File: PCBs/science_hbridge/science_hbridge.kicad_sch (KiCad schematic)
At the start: 34 parts, among them J1 Conn_02x07_Odd_Even, J2 Conn_02x08_Odd_Even, J3 Conn_02x08_Odd_Even, J4 Conn_01x06, J6 Conn_01x02_Pin, J7 Conn_01x04_Pin, J8 Conn_01x06, U1 L298N, U2 MAX485E, U3 NCP718xSN500

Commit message: silkscreen
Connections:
- net 51: no longer R7.2, U2.4 (DI)
- net 52: no longer R12.2, U2.1 (RO)
- net 53: now also R7.2, U2.4 (DI)
- net 54: now also R12.2, U2.1 (RO)
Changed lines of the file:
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@@
 		)
 	)
-	(label "52"
+	(label "54"
 		(at 254 69.85 0)
 		(effects
@@
 		)
 	)
-	(label "51"
+	(label "53"
 		(at 254 77.47 0)
 		(effects

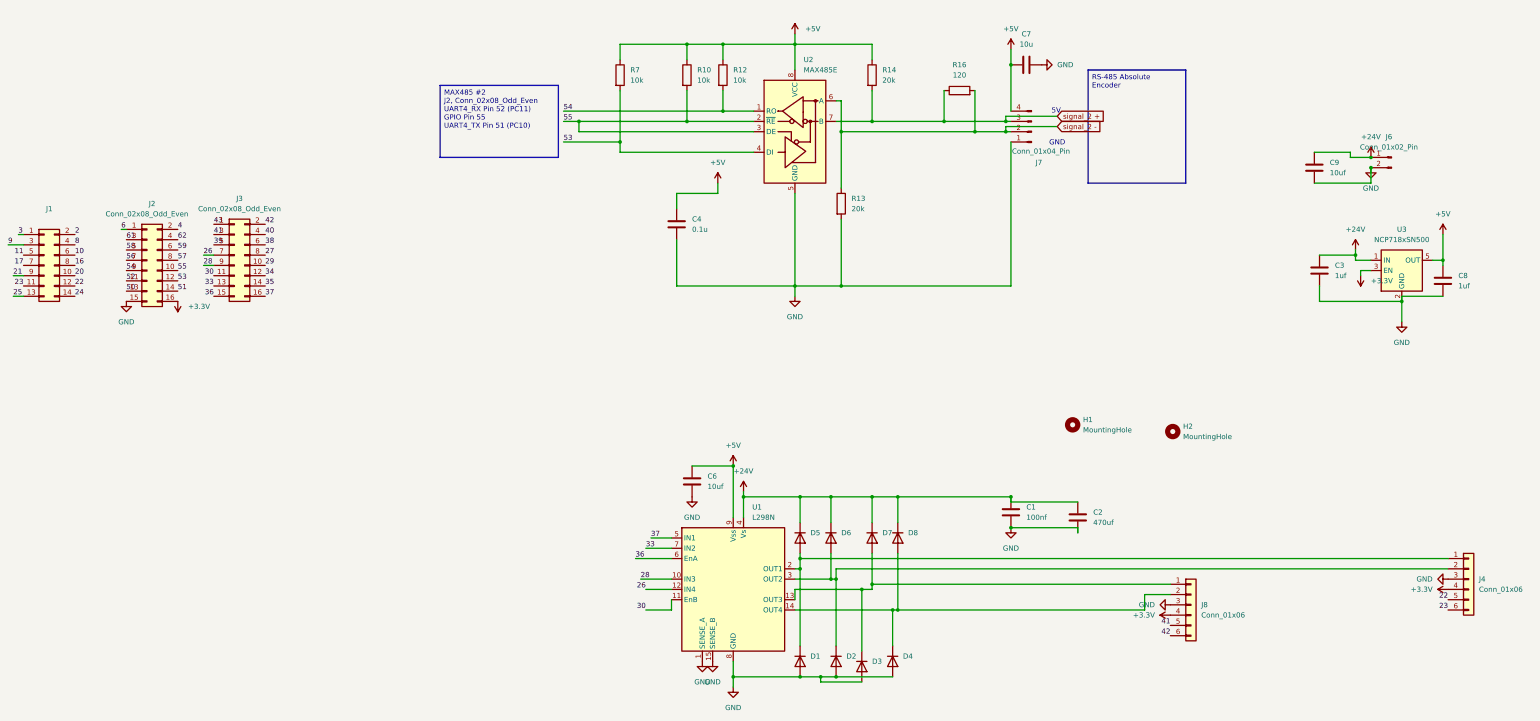
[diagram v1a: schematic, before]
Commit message: fixed 3.3V, fized header
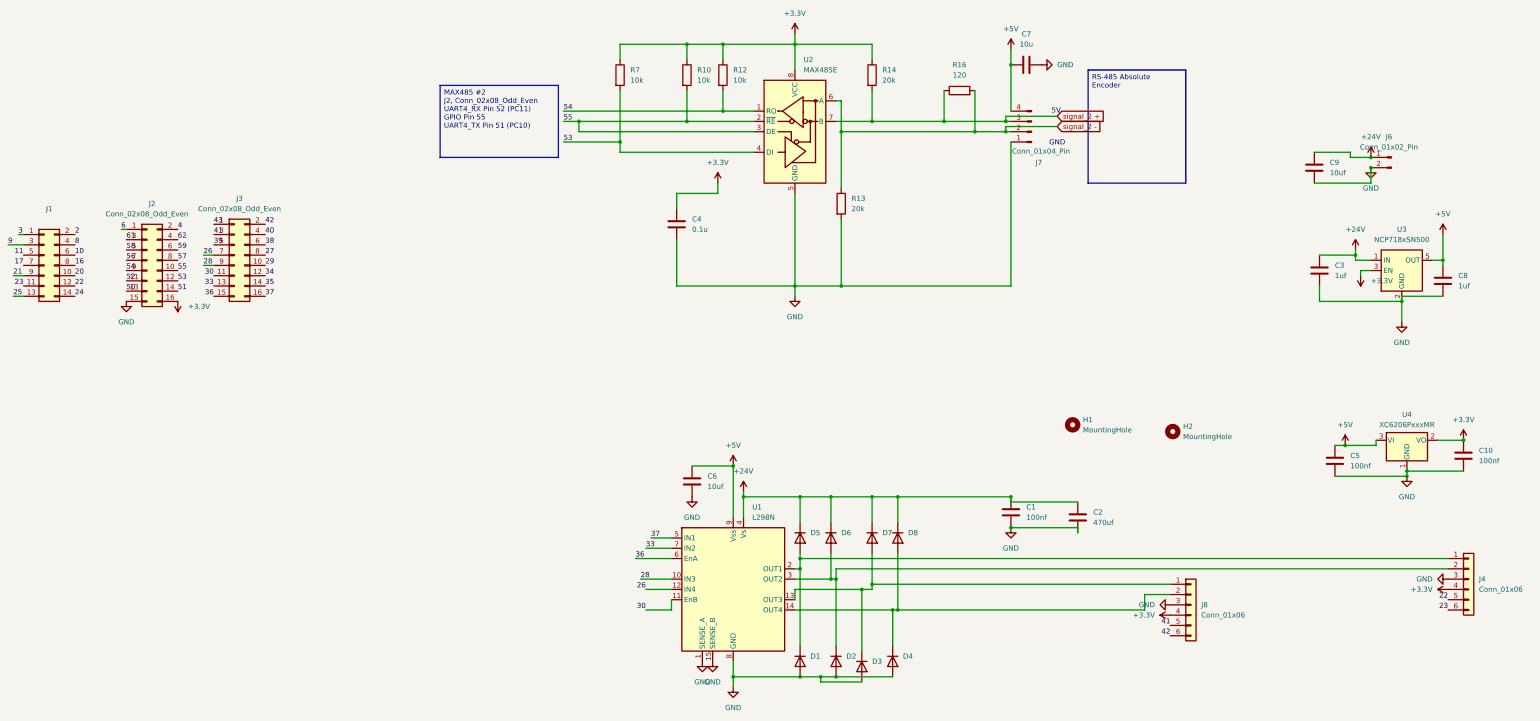
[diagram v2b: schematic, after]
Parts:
- added C10, C5: 100nf, Capacitor_SMD:C_0805_2012Metric_Pad1.18x1.45mm_HandSolder, symbol Device:C
- added U4: XC6206PxxxMR, Package_TO_SOT_SMD:SOT-23-3, symbol Regulator_Linear:XC6206PxxxMR
- J6: footprint Connector_Molex:Molex_Micro-Fit_3.0_43045-0212_2x01_P3.00mm_Vertical -> footprints:CONN_SD-43045-001_02_MOL
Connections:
- net +3.3V: now also C4.1, R10.1, R12.1, R14.1, R7.1, U2.8 (VCC), C10.1, U4.2 (VO)
- net +5V: now also C5.1, U4.3 (VI); no longer C4.1, R10.1, R12.1, R14.1, R7.1, U2.8 (VCC)
- net GND: now also C10.2, C5.2, U4.1 (GND)
